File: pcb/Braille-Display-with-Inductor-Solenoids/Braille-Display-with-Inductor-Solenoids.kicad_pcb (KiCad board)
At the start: 2 copper layers, 90 x 90 mm, 75 parts, among them J1 Screw_Terminal_01x02, J2 Screw_Terminal_01x02, J3 Screw_Terminal_01x02, J4 Conn_01x03, J5 Conn_01x02, J6 Conn_01x08, SW1 SW_Push, SW2 SW_Push, U1 RP2040-Zero, U2 AD116, U26 74HC595, U27 74HC595, U3 AD116, U4 AD116, U5 AD116, U6 AD116, U7 AD116, U8 AD116, U9 AD116

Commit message: WIP: Route one cell
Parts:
- C4, C5, C6, C7, C8, C9: moved to B.Cu
- moved U8 93.8 mm to (69.2, 33.5), turned to 180 degrees
- moved R17 89.5 mm to (70.2, 91.5), turned to 90 degrees
- moved C8 88.6 mm to (69.2, 33.0), turned to -90 degrees
- moved R14 88.5 mm to (69.2, 40.0), turned to -90 degrees
- moved R16 87.9 mm to (68.2, 91.5), turned to 90 degrees
- moved U9 87.2 mm to (69.2, 72.2)
- moved R15 82.5 mm to (69.2, 65.2), turned to 90 degrees
- moved R7 81.9 mm to (58.2, 91.5), turned to 90 degrees
- moved C9 81.6 mm to (69.2, 72.2), turned to 90 degrees
- moved R6 81.0 mm to (56.2, 91.5), turned to 90 degrees
- moved U4 77.4 mm to (57.2, 33.5), turned to 180 degrees
- moved D8 77.1 mm to (69.2, 84.0), turned to 90 degrees
- moved U5 76.8 mm to (57.2, 72.2)
- moved D9 76.5 mm to (69.2, 80.0), turned to 90 degrees
- moved C4 71.9 mm to (57.2, 33.0), turned to -90 degrees
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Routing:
- net /Braille_Cells_and_Controls/Braille_Cell/MAG_BOTTOM_A: track 0.00 -> 19.9 mm, vias 0 -> 1
- net /Braille_Cells_and_Controls/Braille_Cell/MAG_TOP_A: track 0.00 -> 18.5 mm, vias 0 -> 1
- net Net-(L2-Pad2): track 0.00 -> 4.60 mm
- net Net-(L1-Pad2): track 0.00 -> 4.35 mm
- net /Braille_Cells_and_Controls/Braille_Cell/MAG_BOTTOM_B: track 0.00 -> 3.47 mm
- net /Braille_Cells_and_Controls/Braille_Cell/MAG_TOP_B: track 0.00 -> 3.06 mm
- net VDC: vias 5 -> 9
- net GND: vias 10 -> 14

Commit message: WIP: Route more of the board
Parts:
- moved C11 79.9 mm to (75.3, 97.5)
- moved C10 68.3 mm to (61.3, 97.5)
- moved C1 51.1 mm to (118.5, 55.2), turned to 90 degrees
- moved J2 34.8 mm to (82.9, 115.9), turned to 0 degrees
- moved JP1 2.10 mm to (97.0, 105.3), turned to -90 degrees
- moved C4 0.50 mm to (57.2, 33.5), turned to 0 degrees
- moved C6 0.50 mm to (63.2, 33.5), turned to 0 degrees
- moved C8 0.50 mm to (69.2, 33.5), turned to 0 degrees
- turned C5 to 180 degrees
- turned C7 to 180 degrees
- turned C9 to 180 degrees
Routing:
- net /~{SHIFT_OE}: track 28.8 -> 0.00 mm
- net +3V3: track 7.23 -> 32.6 mm, vias 3 -> 8
- net /Braille_Cells_and_Controls/Braille_Cell3/MAG_BOTTOM_A: track 0.00 -> 19.9 mm, vias 0 -> 1
- net /Braille_Cells_and_Controls/Braille_Cell2/MAG_BOTTOM_A: track 0.00 -> 19.9 mm, vias 0 -> 1
- net /Braille_Cells_and_Controls/Braille_Cell1/MAG_BOTTOM_A: track 0.00 -> 19.9 mm, vias 0 -> 1
- net /Braille_Cells_and_Controls/Braille_Cell3/MAG_TOP_A: track 0.00 -> 18.5 mm, vias 0 -> 1
- net /Braille_Cells_and_Controls/Braille_Cell2/MAG_TOP_A: track 0.00 -> 18.5 mm, vias 0 -> 1
- net /Braille_Cells_and_Controls/Braille_Cell1/MAG_TOP_A: track 0.00 -> 18.5 mm, vias 0 -> 1
- net /SW_1: track 12.8 -> 0.00 mm
- net /SW_2: track 10.2 -> 0.00 mm
- net Net-(J3-Pin_1): track 10.4 -> 20.5 mm
- net GND: track 19.1 -> 10.5 mm, vias 14 -> 18
- net Net-(J4-Pin_1): track 7.96 -> 0.00 mm
- net Net-(J4-Pin_3): track 7.32 -> 0.00 mm
- net Net-(J4-Pin_2): track 7.32 -> 0.00 mm
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- added copper zone on B.Cu, net +5V
- added copper zone on B.Cu, net VDC
- removed copper zone on F.Cu, net +5V
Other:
- board text added: "V_IN or 5V"
- board text removed: "5V or V_IN"

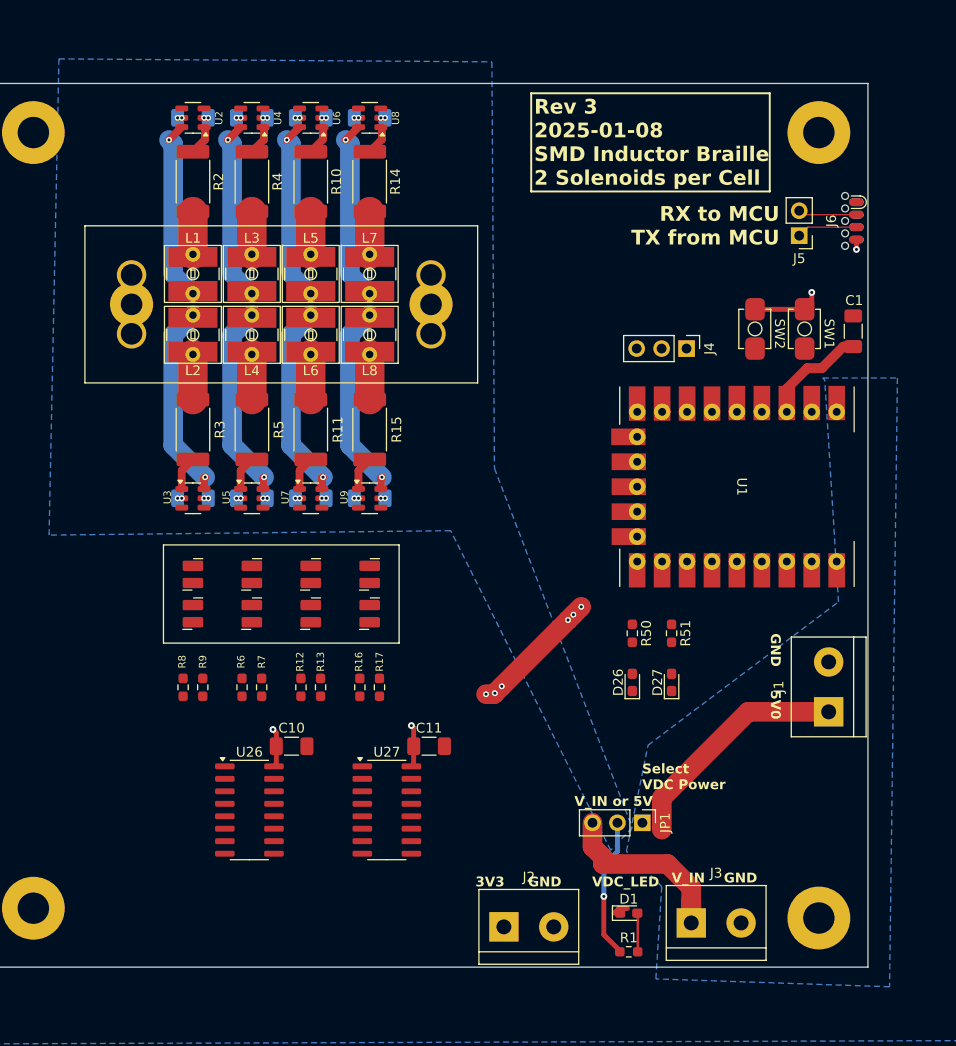
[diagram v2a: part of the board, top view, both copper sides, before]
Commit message: WIP: Swap around power input placement
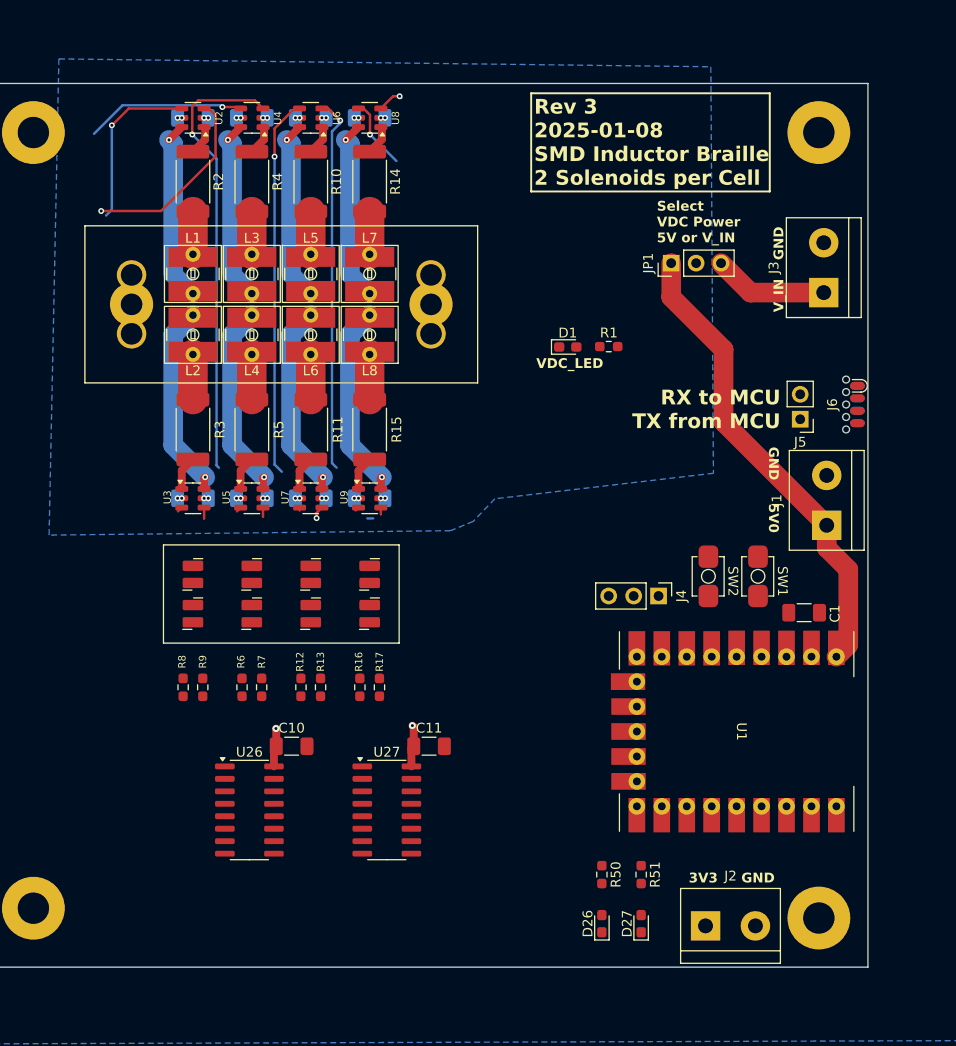
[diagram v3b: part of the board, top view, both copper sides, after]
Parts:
- moved J3 65.6 mm to (115.5, 51.3), turned to 90 degrees
- moved R1 61.7 mm to (93.6, 56.8), turned to 180 degrees
- moved D1 58.0 mm to (89.4, 56.8)
- moved JP1 57.1 mm to (100.0, 48.3), turned to 90 degrees
- moved C1 29.1 mm to (113.5, 83.9), turned to 0 degrees
- moved SW1 25.6 mm to (108.8, 80.2)
- moved SW2 25.6 mm to (103.8, 80.2)
- moved J4 25.4 mm to (98.7, 82.2)
- moved U1 24.9 mm to (93.8, 85.8)
- moved D26 24.8 mm to (92.9, 115.6)
- moved D27 24.8 mm to (96.9, 115.6)
- moved R50 24.8 mm to (92.9, 110.6)
- moved R51 24.8 mm to (96.9, 110.6)
- moved J2 20.5 mm to (103.5, 115.8)
- moved J1 19.0 mm to (115.8, 75.0)
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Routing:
- net /Braille_Cells_and_Controls/CELL1_MAG_TOP_B: track 0.00 -> 45.7 mm, vias 0 -> 1
- net /Braille_Cells_and_Controls/CELL2_MAG_TOP_A: track 0.00 -> 38.7 mm, vias 0 -> 1
- net /Braille_Cells_and_Controls/CELL2_MAG_TOP_B: track 0.00 -> 38.3 mm, vias 0 -> 1
- net +3V3: track 32.6 -> 8.28 mm, vias 8 -> 2
- net +5V: track 24.7 -> 48.1 mm
- net /Braille_Cells_and_Controls/CELL0_MAG_TOP_B: track 0.00 -> 19.6 mm, vias 0 -> 1
- net /Braille_Cells_and_Controls/CELL0_MAG_TOP_A: track 0.00 -> 17.3 mm, vias 0 -> 1
- net /Braille_Cells_and_Controls/CELL1_MAG_TOP_A: track 0.00 -> 16.3 mm, vias 0 -> 1
- net VDC: track 14.4 -> 0.00 mm, vias 17 -> 16
- net GND: track 10.5 -> 0.00 mm, vias 18 -> 16
- net Net-(J3-Pin_1): track 20.5 -> 11.7 mm
- net /UART0_TX: track 7.76 -> 0.00 mm
- net /UART0_RX: track 7.57 -> 0.00 mm
- net /Braille_Cells_and_Controls/CELL3_MAG_TOP_A: track 0.00 -> 7.25 mm, vias 0 -> 1
- net Net-(D1-A): track 3.96 -> 0.00 mm
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- removed copper zone on B.Cu, net +5V
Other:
- board text added: "Select VDC Power 5V or V_IN"
- board text removed: "Select VDC Power"
- board text removed: "V_IN or 5V"

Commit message: Finish and polish design
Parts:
- moved H1 3.00 mm to (35.0, 32.0)
- moved H2 3.00 mm to (115.0, 32.0)
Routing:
- net GND: track 0.00 -> 282.7 mm, vias 16 -> 32
- net +3V3: track 8.28 -> 121.9 mm, vias 2 -> 10
- net VDC: track 0.00 -> 101.3 mm, vias 16 -> 23
- net /Braille_Cells_and_Controls/CELL0_MAG_TOP_A: track 17.3 -> 113.9 mm, vias 1 -> 3
- net /Braille_Cells_and_Controls/CELL1_MAG_TOP_A: track 16.3 -> 105.3 mm, vias 1 -> 0
- net /Braille_Cells_and_Controls/CELL3_MAG_TOP_B: track 2.69 -> 85.2 mm, vias 1 -> 3
- net /Braille_Cells_and_Controls/CELL3_MAG_TOP_A: track 7.25 -> 84.7 mm, vias 1 -> 3
- net /Braille_Cells_and_Controls/CELL2_MAG_TOP_A: track 38.7 -> 109.7 mm, vias 1 -> 7
- net /Braille_Cells_and_Controls/CELL0_MAG_TOP_B: track 19.6 -> 88.4 mm, vias 1 -> 2
- net /SHIFT_SER_IN: track 0.60 -> 63.4 mm, vias 0 -> 2
- net /SHIFT_SRCK: track 0.00 -> 56.2 mm
- net /SHIFT_RCLK: track 0.00 -> 53.5 mm, vias 0 -> 1
- net /~{SHIFT_SRCLR}: track 0.00 -> 52.8 mm
- net /~{SHIFT_OE}: track 0.00 -> 52.2 mm, vias 0 -> 1
- net /UART0_RX: track 0.00 -> 52.1 mm
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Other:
- board size 90 x 90 mm -> 90 x 93 mm
- board text added: "Rev 3 2025-01-05 SMD Inductor Braille 2 Solenoids per Cell"
- board text removed: "Rev 3 2025-01-08 SMD Inductor Braille 2 Solenoids per Cell"

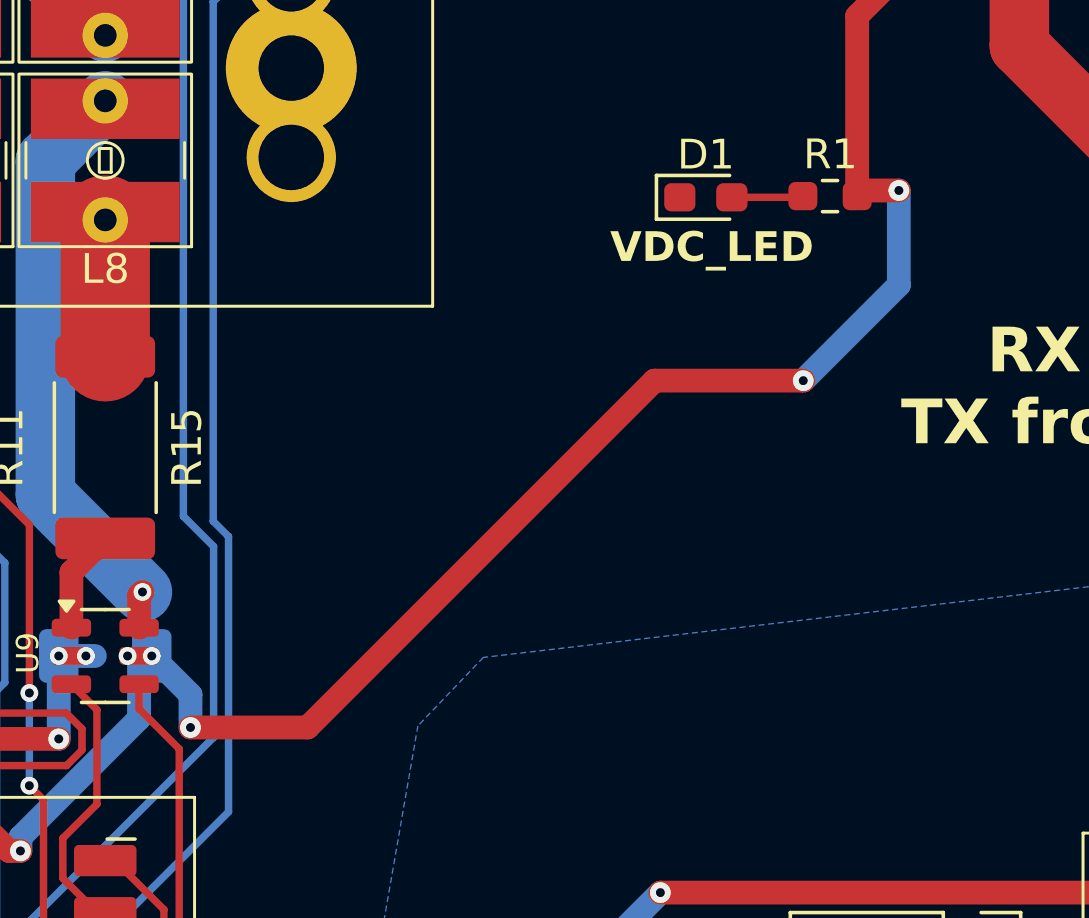
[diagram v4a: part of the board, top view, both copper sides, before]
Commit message: Bit of tiny routing, export production file
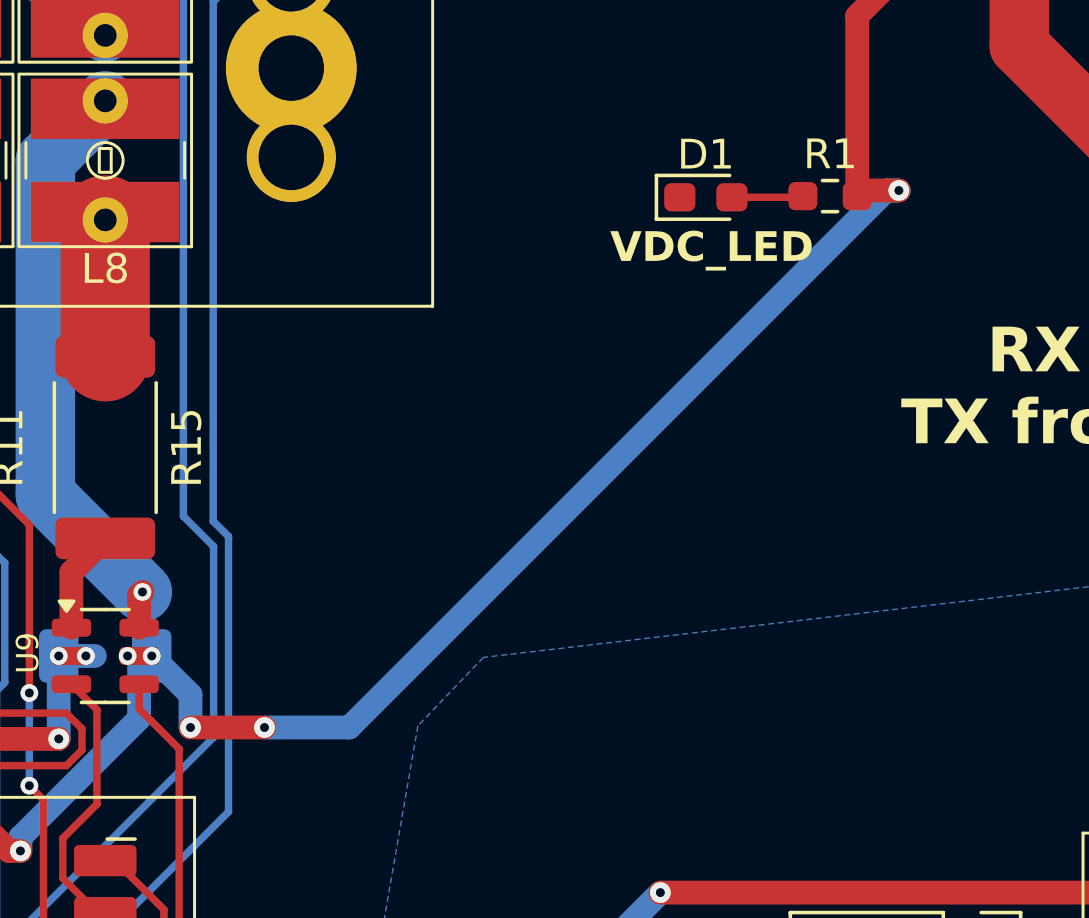
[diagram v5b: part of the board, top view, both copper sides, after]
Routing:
- net VDC: track 101.3 -> 99.5 mm

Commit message: pcb: WIP - Switch to new parts, layout
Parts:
- removed J3: Screw_Terminal_01x02, TerminalBlock:TerminalBlock_bornier-2_P5.08mm
- removed JP1: SolderJumper_3_Open, Connector_PinHeader_2.54mm:PinHeader_1x03_P2.54mm_Vertical
- removed R10, R11, R14, R15, R2, R3, R4, R5: 20, Resistor_SMD:R_2512_6332Metric_Pad1.40x3.35mm_HandSolder
- removed SW1, SW2: SW_Push, 00-project-footprints:PushButtonSMD_2.93x3.9
- added C103: 100n, Capacitor_SMD:C_0603_1608Metric_Pad1.08x0.95mm_HandSolder, F.Cu at (181.8, 63.2)
- added C12: 10u, Capacitor_SMD:C_1206_3216Metric_Pad1.33x1.80mm_HandSolder, F.Cu at (108.0, 48.9)
- added C13: 10u, Capacitor_SMD:C_1206_3216Metric_Pad1.33x1.80mm_HandSolder, F.Cu at (161.8, 67.5)
- added J7: Screw_Terminal_01x02, TerminalBlock:TerminalBlock_bornier-2_P5.08mm, F.Cu at (116.0, 46.5)
- added J8: Barrel_Jack_Switch, Connector_BarrelJack:BarrelJack_Horizontal, F.Cu at (91.0, 113.5)
- added R103: R, Resistor_SMD:R_1206_3216Metric_Pad1.30x1.75mm_HandSolder, F.Cu at (171.0, 72.7)
- added R105: 5k1, Resistor_SMD:R_0603_1608Metric_Pad0.98x0.95mm_HandSolder, F.Cu at (181.8, 65.7)
- added R106: 5k1, Resistor_SMD:R_0603_1608Metric_Pad0.98x0.95mm_HandSolder, F.Cu at (181.8, 68.2)
- added R107: 5k1, Resistor_SMD:R_0603_1608Metric_Pad0.98x0.95mm_HandSolder, F.Cu at (51.8, 37.0)
- added R108: 5k1, Resistor_SMD:R_0603_1608Metric_Pad0.98x0.95mm_HandSolder, F.Cu at (198.6, 50.6)
- added R109: 5k1, Resistor_SMD:R_0603_1608Metric_Pad0.98x0.95mm_HandSolder, F.Cu at (185.9, 79.0)
- added R110: 5k1, Resistor_SMD:R_0603_1608Metric_Pad0.98x0.95mm_HandSolder, F.Cu at (170.2, 79.0)
- added R111: 5k1, Resistor_SMD:R_0603_1608Metric_Pad0.98x0.95mm_HandSolder, F.Cu at (51.8, 47.5)
- added R112: 5k1, Resistor_SMD:R_0603_1608Metric_Pad0.98x0.95mm_HandSolder, F.Cu at (198.6, 53.1)
- added R113: 5k1, Resistor_SMD:R_0603_1608Metric_Pad0.98x0.95mm_HandSolder, F.Cu at (185.9, 81.5)
- added R114: 5k1, Resistor_SMD:R_0603_1608Metric_Pad0.98x0.95mm_HandSolder, F.Cu at (170.2, 81.5)
- added R115: 5k1, Resistor_SMD:R_0603_1608Metric_Pad0.98x0.95mm_HandSolder, F.Cu at (51.2, 98.2)
- added R116: 5k1, Resistor_SMD:R_0603_1608Metric_Pad0.98x0.95mm_HandSolder, F.Cu at (198.6, 55.6)
- added R117: 5k1, Resistor_SMD:R_0603_1608Metric_Pad0.98x0.95mm_HandSolder, F.Cu at (185.9, 84.0)
- added R118: 5k1, Resistor_SMD:R_0603_1608Metric_Pad0.98x0.95mm_HandSolder, F.Cu at (170.2, 84.0)
- added R119: 5k1, Resistor_SMD:R_0603_1608Metric_Pad0.98x0.95mm_HandSolder, F.Cu at (51.2, 109.5)
- added R120: 5k1, Resistor_SMD:R_0603_1608Metric_Pad0.98x0.95mm_HandSolder, F.Cu at (198.6, 58.1)
- added R121: 5k1, Resistor_SMD:R_0603_1608Metric_Pad0.98x0.95mm_HandSolder, F.Cu at (185.9, 86.5)
- added R122: 5k1, Resistor_SMD:R_0603_1608Metric_Pad0.98x0.95mm_HandSolder, F.Cu at (170.2, 86.5)
- added S1: Tactile Button, 160gf, PCM_JLCPCB:SW-SMD_4P-L5.1-W5.1-P3.70-LS6.5-TL-2, F.Cu at (163.4, 52.6)
- added S10: Tactile Button, 160gf, PCM_JLCPCB:SW-SMD_4P-L5.1-W5.1-P3.70-LS6.5-TL-2, F.Cu at (163.4, 87.5)
- added S11: Tactile Button, 160gf, PCM_JLCPCB:SW-SMD_4P-L5.1-W5.1-P3.70-LS6.5-TL-2, F.Cu at (51.2, 103.5)
- added S12: Tactile Button, 160gf, PCM_JLCPCB:SW-SMD_4P-L5.1-W5.1-P3.70-LS6.5-TL-2, F.Cu at (51.2, 115.0)
- added S13: Tactile Button, 160gf, PCM_JLCPCB:SW-SMD_4P-L5.1-W5.1-P3.70-LS6.5-TL-2, F.Cu at (191.8, 65.7)
- added S14: Tactile Button, 160gf, PCM_JLCPCB:SW-SMD_4P-L5.1-W5.1-P3.70-LS6.5-TL-2, F.Cu at (191.8, 72.3)
- added S15: Tactile Button, 160gf, PCM_JLCPCB:SW-SMD_4P-L5.1-W5.1-P3.70-LS6.5-TL-2, F.Cu at (179.1, 94.1)
- added S16: Tactile Button, 160gf, PCM_JLCPCB:SW-SMD_4P-L5.1-W5.1-P3.70-LS6.5-TL-2, F.Cu at (179.1, 100.7)
- added S17: Tactile Button, 160gf, PCM_JLCPCB:SW-SMD_4P-L5.1-W5.1-P3.70-LS6.5-TL-2, F.Cu at (163.4, 94.1)
- added S18: Tactile Button, 160gf, PCM_JLCPCB:SW-SMD_4P-L5.1-W5.1-P3.70-LS6.5-TL-2, F.Cu at (163.4, 100.7)
- added S2: Tactile Button, 160gf, PCM_JLCPCB:SW-SMD_4P-L5.1-W5.1-P3.70-LS6.5-TL-2, F.Cu at (163.4, 59.2)
- added S3: Tactile Button, 160gf, PCM_JLCPCB:SW-SMD_4P-L5.1-W5.1-P3.70-LS6.5-TL-2, F.Cu at (51.2, 32.0)
- added S4: Tactile Button, 160gf, PCM_JLCPCB:SW-SMD_4P-L5.1-W5.1-P3.70-LS6.5-TL-2, F.Cu at (191.8, 52.6)
- added S5: Tactile Button, 160gf, PCM_JLCPCB:SW-SMD_4P-L5.1-W5.1-P3.70-LS6.5-TL-2, F.Cu at (179.1, 81.0)
- added S6: Tactile Button, 160gf, PCM_JLCPCB:SW-SMD_4P-L5.1-W5.1-P3.70-LS6.5-TL-2, F.Cu at (163.4, 81.0)
- added S7: Tactile Button, 160gf, PCM_JLCPCB:SW-SMD_4P-L5.1-W5.1-P3.70-LS6.5-TL-2, F.Cu at (51.2, 42.2)
- added S8: Tactile Button, 160gf, PCM_JLCPCB:SW-SMD_4P-L5.1-W5.1-P3.70-LS6.5-TL-2, F.Cu at (191.8, 59.2)
- added S9: Tactile Button, 160gf, PCM_JLCPCB:SW-SMD_4P-L5.1-W5.1-P3.70-LS6.5-TL-2, F.Cu at (179.1, 87.5)
- added U103: INA219AxD, Package_SO:SOIC-8_3.9x4.9mm_P1.27mm, F.Cu at (100.0, 48.6)
- C10, C11: footprint Capacitor_SMD:C_1206_3216Metric_Pad1.33x1.80mm_HandSolder -> Capacitor_SMD:C_0603_1608Metric_Pad1.08x0.95mm_HandSolder
- U2, U3, U4, U5, U6, U7, U8, U9: value AD116 -> EG27324; footprint Package_TO_SOT_SMD:SOT-23-6 -> Package_SO:SOP-8_3.9x4.9mm_P1.27mm
- moved R12 82.8 mm to (143.2, 108.6)
- moved R13 82.8 mm to (145.2, 108.6)
- moved R16 82.8 mm to (149.2, 108.6)
- moved R17 82.8 mm to (151.2, 108.6)
- moved R6 82.8 mm to (137.2, 108.6)
- moved R7 82.8 mm to (139.2, 108.6)
- moved R8 32.0 mm to (51.2, 59.5), turned to 0 degrees
- moved D4 31.3 mm to (87.5, 75.9)
- moved D5 31.3 mm to (87.5, 71.9)
- moved D6 31.3 mm to (93.5, 75.9)
- moved D7 31.3 mm to (93.5, 71.9)
- moved D8 31.3 mm to (99.5, 75.9)
- moved D9 31.3 mm to (99.5, 71.9)
- moved D2 22.0 mm to (51.2, 62.0), turned to 0 degrees
- moved U26 21.3 mm to (36.5, 98.1)
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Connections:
- D2 pad 1: /Braille_Cells_and_Controls/CELL0_MAG_TOP_B -> /Braille_Cells_and_Controls/Braille_Cell/MAG_TOP_B
- D3 pad 1: /Braille_Cells_and_Controls/CELL0_MAG_BOTTOM_B -> /Braille_Cells_and_Controls/Braille_Cell/MAG_BOTTOM_B
- D4 pad 1: /Braille_Cells_and_Controls/CELL1_MAG_TOP_B -> /Braille_Cells_and_Controls/Braille_Cell1/MAG_TOP_B
- D5 pad 1: /Braille_Cells_and_Controls/CELL1_MAG_BOTTOM_B -> /Braille_Cells_and_Controls/Braille_Cell1/MAG_BOTTOM_B
- D6 pad 1: /Braille_Cells_and_Controls/CELL2_MAG_TOP_B -> /Braille_Cells_and_Controls/Braille_Cell2/MAG_TOP_B
- D7 pad 1: /Braille_Cells_and_Controls/CELL2_MAG_BOTTOM_B -> /Braille_Cells_and_Controls/Braille_Cell2/MAG_BOTTOM_B
- D8 pad 1: /Braille_Cells_and_Controls/CELL3_MAG_TOP_B -> /Braille_Cells_and_Controls/Braille_Cell3/MAG_TOP_B
- D9 pad 1: /Braille_Cells_and_Controls/CELL3_MAG_BOTTOM_B -> /Braille_Cells_and_Controls/Braille_Cell3/MAG_BOTTOM_B
- L1 pad 2: Net-(L1-Pad2) -> /Braille_Cells_and_Controls/Braille_Cell/MAG_TOP_B
- L2 pad 2: Net-(L2-Pad2) -> /Braille_Cells_and_Controls/Braille_Cell/MAG_BOTTOM_B
- L3 pad 2: Net-(L3-Pad2) -> /Braille_Cells_and_Controls/Braille_Cell1/MAG_TOP_B
- L4 pad 2: Net-(L4-Pad2) -> /Braille_Cells_and_Controls/Braille_Cell1/MAG_BOTTOM_B
- L5 pad 2: Net-(L5-Pad2) -> /Braille_Cells_and_Controls/Braille_Cell2/MAG_TOP_B
- L6 pad 2: Net-(L6-Pad2) -> /Braille_Cells_and_Controls/Braille_Cell2/MAG_BOTTOM_B
- L7 pad 2: Net-(L7-Pad2) -> /Braille_Cells_and_Controls/Braille_Cell3/MAG_TOP_B
- L8 pad 2: Net-(L8-Pad2) -> /Braille_Cells_and_Controls/Braille_Cell3/MAG_BOTTOM_B
- R12 pad 1: /Braille_Cells_and_Controls/CELL2_MAG_TOP_A -> /Braille_Cells_and_Controls/Braille_Cell2/MAG_TOP_A
- R13 pad 1: /Braille_Cells_and_Controls/CELL2_MAG_BOTTOM_A -> /Braille_Cells_and_Controls/Braille_Cell2/MAG_BOTTOM_A
- R16 pad 1: /Braille_Cells_and_Controls/CELL3_MAG_TOP_A -> /Braille_Cells_and_Controls/Braille_Cell3/MAG_TOP_A
- R17 pad 1: /Braille_Cells_and_Controls/CELL3_MAG_BOTTOM_A -> /Braille_Cells_and_Controls/Braille_Cell3/MAG_BOTTOM_A
- R6 pad 1: /Braille_Cells_and_Controls/CELL1_MAG_TOP_A -> /Braille_Cells_and_Controls/Braille_Cell1/MAG_TOP_A
- R7 pad 1: /Braille_Cells_and_Controls/CELL1_MAG_BOTTOM_A -> /Braille_Cells_and_Controls/Braille_Cell1/MAG_BOTTOM_A
- R8 pad 1: /Braille_Cells_and_Controls/CELL0_MAG_TOP_A -> /Braille_Cells_and_Controls/Braille_Cell/MAG_TOP_A
- R9 pad 1: /Braille_Cells_and_Controls/CELL0_MAG_BOTTOM_A -> /Braille_Cells_and_Controls/Braille_Cell/MAG_BOTTOM_A
- U2 pad 1: /Braille_Cells_and_Controls/Braille_Cell/MAG_TOP_B -> unconnected-(U2-NC-Pad1)
- U2 pad 2: GND -> /Braille_Cells_and_Controls/Braille_Cell/MAG_TOP_SW_A
- U2 pad 3: /Braille_Cells_and_Controls/CELL0_MAG_TOP_B -> GND
- U2 pad 4: /Braille_Cells_and_Controls/CELL0_MAG_TOP_A -> /Braille_Cells_and_Controls/Braille_Cell/MAG_TOP_SW_B
- U2 pad 5: VDC -> /Braille_Cells_and_Controls/Braille_Cell/MAG_TOP_B
- U2 pad 6: /Braille_Cells_and_Controls/Braille_Cell/MAG_TOP_A -> VDC
- U3 pad 1: /Braille_Cells_and_Controls/Braille_Cell/MAG_BOTTOM_B -> unconnected-(U3-NC-Pad1)
- U3 pad 2: GND -> /Braille_Cells_and_Controls/Braille_Cell/MAG_BOTTOM_SW_A
- U3 pad 3: /Braille_Cells_and_Controls/CELL0_MAG_BOTTOM_B -> GND
- U3 pad 4: /Braille_Cells_and_Controls/CELL0_MAG_BOTTOM_A -> /Braille_Cells_and_Controls/Braille_Cell/MAG_BOTTOM_SW_B
- U3 pad 5: VDC -> /Braille_Cells_and_Controls/Braille_Cell/MAG_BOTTOM_B
- U3 pad 6: /Braille_Cells_and_Controls/Braille_Cell/MAG_BOTTOM_A -> VDC
- U4 pad 1: /Braille_Cells_and_Controls/Braille_Cell1/MAG_TOP_B -> unconnected-(U4-NC-Pad1)
- U4 pad 2: GND -> /Braille_Cells_and_Controls/Braille_Cell1/MAG_TOP_SW_A
- U4 pad 3: /Braille_Cells_and_Controls/CELL1_MAG_TOP_B -> GND
- U4 pad 4: /Braille_Cells_and_Controls/CELL1_MAG_TOP_A -> /Braille_Cells_and_Controls/Braille_Cell1/MAG_TOP_SW_B
- U4 pad 5: VDC -> /Braille_Cells_and_Controls/Braille_Cell1/MAG_TOP_B
- U4 pad 6: /Braille_Cells_and_Controls/Braille_Cell1/MAG_TOP_A -> VDC
- U5 pad 1: /Braille_Cells_and_Controls/Braille_Cell1/MAG_BOTTOM_B -> unconnected-(U5-NC-Pad1)
- U5 pad 2: GND -> /Braille_Cells_and_Controls/Braille_Cell1/MAG_BOTTOM_SW_A
- U5 pad 3: /Braille_Cells_and_Controls/CELL1_MAG_BOTTOM_B -> GND
- U5 pad 4: /Braille_Cells_and_Controls/CELL1_MAG_BOTTOM_A -> /Braille_Cells_and_Controls/Braille_Cell1/MAG_BOTTOM_SW_B
- U5 pad 5: VDC -> /Braille_Cells_and_Controls/Braille_Cell1/MAG_BOTTOM_B
- U5 pad 6: /Braille_Cells_and_Controls/Braille_Cell1/MAG_BOTTOM_A -> VDC
- U6 pad 1: /Braille_Cells_and_Controls/Braille_Cell2/MAG_TOP_B -> unconnected-(U6-NC-Pad1)
- U6 pad 2: GND -> /Braille_Cells_and_Controls/Braille_Cell2/MAG_TOP_SW_A
- U6 pad 3: /Braille_Cells_and_Controls/CELL2_MAG_TOP_B -> GND
- U6 pad 4: /Braille_Cells_and_Controls/CELL2_MAG_TOP_A -> /Braille_Cells_and_Controls/Braille_Cell2/MAG_TOP_SW_B
- U6 pad 5: VDC -> /Braille_Cells_and_Controls/Braille_Cell2/MAG_TOP_B
- U6 pad 6: /Braille_Cells_and_Controls/Braille_Cell2/MAG_TOP_A -> VDC
- U7 pad 1: /Braille_Cells_and_Controls/Braille_Cell2/MAG_BOTTOM_B -> unconnected-(U7-NC-Pad1)
- U7 pad 2: GND -> /Braille_Cells_and_Controls/Braille_Cell2/MAG_BOTTOM_SW_A
- U7 pad 3: /Braille_Cells_and_Controls/CELL2_MAG_BOTTOM_B -> GND
- U7 pad 4: /Braille_Cells_and_Controls/CELL2_MAG_BOTTOM_A -> /Braille_Cells_and_Controls/Braille_Cell2/MAG_BOTTOM_SW_B
- U7 pad 5: VDC -> /Braille_Cells_and_Controls/Braille_Cell2/MAG_BOTTOM_B
- U7 pad 6: /Braille_Cells_and_Controls/Braille_Cell2/MAG_BOTTOM_A -> VDC
- U8 pad 1: /Braille_Cells_and_Controls/Braille_Cell3/MAG_TOP_B -> unconnected-(U8-NC-Pad1)
- U8 pad 2: GND -> /Braille_Cells_and_Controls/Braille_Cell3/MAG_TOP_SW_A
- U8 pad 3: /Braille_Cells_and_Controls/CELL3_MAG_TOP_B -> GND
- U8 pad 4: /Braille_Cells_and_Controls/CELL3_MAG_TOP_A -> /Braille_Cells_and_Controls/Braille_Cell3/MAG_TOP_SW_B
- U8 pad 5: VDC -> /Braille_Cells_and_Controls/Braille_Cell3/MAG_TOP_B
- U8 pad 6: /Braille_Cells_and_Controls/Braille_Cell3/MAG_TOP_A -> VDC
- U9 pad 1: /Braille_Cells_and_Controls/Braille_Cell3/MAG_BOTTOM_B -> unconnected-(U9-NC-Pad1)
- U9 pad 2: GND -> /Braille_Cells_and_Controls/Braille_Cell3/MAG_BOTTOM_SW_A
- U9 pad 3: /Braille_Cells_and_Controls/CELL3_MAG_BOTTOM_B -> GND
- U9 pad 4: /Braille_Cells_and_Controls/CELL3_MAG_BOTTOM_A -> /Braille_Cells_and_Controls/Braille_Cell3/MAG_BOTTOM_SW_B
- U9 pad 5: VDC -> /Braille_Cells_and_Controls/Braille_Cell3/MAG_BOTTOM_B
- U9 pad 6: /Braille_Cells_and_Controls/Braille_Cell3/MAG_BOTTOM_A -> VDC
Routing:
- net GND: track 282.7 -> 0.00 mm, vias 32 -> 0
- net +3V3: track 121.9 -> 0.00 mm, vias 10 -> 0
- net /Braille_Cells_and_Controls/CELL0_MAG_TOP_A: track 113.9 -> 0.00 mm, vias 3 -> 0
- net /Braille_Cells_and_Controls/CELL2_MAG_TOP_A: track 109.7 -> 0.00 mm, vias 7 -> 0
- net /Braille_Cells_and_Controls/CELL1_MAG_TOP_A: track 105.3 -> 0.00 mm
- net VDC: track 99.5 -> 0.00 mm, vias 23 -> 0
- net /Braille_Cells_and_Controls/CELL0_MAG_TOP_B: track 88.4 -> 0.00 mm, vias 2 -> 0
- net /Braille_Cells_and_Controls/CELL3_MAG_TOP_B: track 85.2 -> 0.00 mm, vias 3 -> 0
- net /Braille_Cells_and_Controls/CELL3_MAG_TOP_A: track 84.7 -> 0.00 mm, vias 3 -> 0
- net /Braille_Cells_and_Controls/CELL2_MAG_TOP_B: track 79.7 -> 0.00 mm, vias 4 -> 0
- net /Braille_Cells_and_Controls/CELL1_MAG_TOP_B: track 78.8 -> 0.00 mm, vias 2 -> 0
- net /SHIFT_SER_IN: track 63.4 -> 0.00 mm, vias 2 -> 0
- net /SHIFT_SRCK: track 56.2 -> 0.00 mm
- net /SHIFT_RCLK: track 53.5 -> 0.00 mm, vias 1 -> 0
- net /~{SHIFT_SRCLR}: track 52.8 -> 0.00 mm
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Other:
- board text added: "GND VIN"
- board text added: "Type 3 Rev (4) 2025-xx-xx SMD Inductor Braille 2 Solenoids per Cell"
- board text removed: "Rev 3 2025-01-05 SMD Inductor Braille 2 Solenoids per Cell"
- board text removed: "Select VDC Power 5V or V_IN"
- board text removed: "V_IN GND"
